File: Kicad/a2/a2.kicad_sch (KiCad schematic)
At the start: 123 parts, among them J1 Conn_02x03_Odd_Even, J2 VGA, J3 AudioJack4, J4 Conn_02x17_Odd_Even, J6 Barrel Jack, J7 DE9_Plug, J8 DE9_Plug, SW1 Q, SW10 P, SW11 A, SW12 S, SW13 D, SW14 F, SW15 G, SW16 H, SW17 J, SW18 K, SW19 L, SW2 W, SW20 ENT, SW21 SHIFT, SW22 Z, SW23 X, SW24 C, SW25 V, SW26 B, SW27 N, SW28 M, SW29 SPACE, SW3 E, SW30 ALT, SW31 SW_Push, SW32 SW_SPDT, SW4 R, SW5 T, SW6 Y, SW7 U, SW8 I, SW9 O, U1 74HC590A, U10 74HC32, U11 74HC174, U12 74HC4520, U2 74HC590A, U3 62256, U4 SST39SF0x0, U5 W65C02SxP, U6 74HCT540, U7 74HC166, U8 74HC14, U9 74HC10, Y1 16Mhz

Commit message: add 2 more m2 screw posts
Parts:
- removed BZ1: Buzzer, Buzzer_Beeper:MagneticBuzzer_Kingstate_KCG0601, symbol Device:Buzzer
- added H5, H6: M2, MountingHole:MountingHole_2.2mm_M2_ISO7380_Pad, symbol Mechanical:MountingHole_Pad
- added LS1: Speaker, Connector_Molex:Molex_PicoBlade_53047-0210_1x02_P1.25mm_Vertical, symbol Device:Speaker
- C16: footprint PCM_Capacitor_THT_AKL:CP_Radial_D5.0mm_P2.00mm -> PCM_Capacitor_THT_AKL:CP_Radial_D4.0mm_P1.50mm
- C17: value 100nF -> 47nF
- H1, H2, H3, H4: value MountingHole_Pad -> M2; now in the parts list
- RN1: value R_Network06 -> 10KΩ
- RN2, RN3: value R_Network04 -> 1KΩ
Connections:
- net DataOut: no longer R6.2
- net GND: now also H5.1, H6.1, LS1.2; no longer C17.2
- net Speaker: now also LS1.1
- net AUDIN renamed DataIn
- new net: C17.2, R6.2
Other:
- moved on the sheet: C13, H1, H2, H3, H4, R6, RN3, SW1, SW10, SW11, SW12, SW13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

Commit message: Big a2 update
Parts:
- removed C14: 100nF, PCM_Capacitor_THT_AKL_Double:C_Disc_D3.0mm_W1.6mm_P2.50mm, symbol Device:C_Small
- removed C3: 4.7µF, PCM_Capacitor_THT_AKL:CP_Radial_D4.0mm_P1.50mm, symbol PCM_Capacitor_AKL:CP_Radial_D5.0mm_P2.00mm
- removed D10, D11, D12, D13, D14, D15, D16, D17, D18, D19, D20, D21, D22, D23, D24, D25, D26, D27, D28, D29, D30, D31, D32, D33, D34, D35, D36, D7, D8, D9: 1N4148, PCM_Diode_THT_AKL_Double:D_DO-35_SOD27_P7.62mm_Horizontal, symbol PCM_Diode_AKL:1N4148
- removed J7, J8: DE9_Plug, Smal:DSUB9-Atari, symbol Connector:DE9_Plug
- removed R3, R4: 27KΩ, PCM_Resistor_THT_AKL_Double:R_Axial_DIN0204_L3.6mm_D1.6mm_P7.62mm_Horizontal, symbol Device:R
- removed R5: 5.6KΩ, PCM_Resistor_THT_AKL_Double:R_Axial_DIN0204_L3.6mm_D1.6mm_P7.62mm_Horizontal, symbol Device:R
- removed RN1: 10KΩ, Resistor_THT:R_Array_SIP7, symbol Device:R_Network06
- removed SW1: Q, MicroMicro:SW_Redragon_MX_LowProfile_PCB_1.00u_Other, symbol Switch:SW_Push_45deg
- removed SW10: P, MicroMicro:SW_Redragon_MX_LowProfile_PCB_1.00u_Other, symbol Switch:SW_Push_45deg
- removed SW11: A, MicroMicro:SW_Redragon_MX_LowProfile_PCB_1.00u_Other, symbol Switch:SW_Push_45deg
- removed SW12: S, MicroMicro:SW_Redragon_MX_LowProfile_PCB_1.00u_Other, symbol Switch:SW_Push_45deg
- removed SW13: D, MicroMicro:SW_Redragon_MX_LowProfile_PCB_1.00u_Other, symbol Switch:SW_Push_45deg
- removed SW14: F, MicroMicro:SW_Redragon_MX_LowProfile_PCB_1.00u_Other, symbol Switch:SW_Push_45deg
- removed SW15: G, MicroMicro:SW_Redragon_MX_LowProfile_PCB_1.00u_Other, symbol Switch:SW_Push_45deg
- removed SW16: H, MicroMicro:SW_Redragon_MX_LowProfile_PCB_1.00u_Other, symbol Switch:SW_Push_45deg
- removed SW17: J, MicroMicro:SW_Redragon_MX_LowProfile_PCB_1.00u_Other, symbol Switch:SW_Push_45deg
- removed SW18: K, MicroMicro:SW_Redragon_MX_LowProfile_PCB_1.00u_Other, symbol Switch:SW_Push_45deg
- removed SW19: L, MicroMicro:SW_Redragon_MX_LowProfile_PCB_1.00u_Other, symbol Switch:SW_Push_45deg
- removed SW2: W, MicroMicro:SW_Redragon_MX_LowProfile_PCB_1.00u_Other, symbol Switch:SW_Push_45deg
- removed SW20: ENT, MicroMicro:SW_Redragon_MX_LowProfile_PCB_1.00u_Other, symbol Switch:SW_Push_45deg
- removed SW21: SHIFT, MicroMicro:SW_Redragon_MX_LowProfile_PCB_1.00u_Other, symbol Switch:SW_Push_45deg
- removed SW22: Z, MicroMicro:SW_Redragon_MX_LowProfile_PCB_1.00u_Other, symbol Switch:SW_Push_45deg
- removed SW23: X, MicroMicro:SW_Redragon_MX_LowProfile_PCB_1.00u_Other, symbol Switch:SW_Push_45deg
- removed SW24: C, MicroMicro:SW_Redragon_MX_LowProfile_PCB_1.00u_Other, symbol Switch:SW_Push_45deg
- removed SW25: V, MicroMicro:SW_Redragon_MX_LowProfile_PCB_1.00u_Other, symbol Switch:SW_Push_45deg
- removed SW26: B, MicroMicro:SW_Redragon_MX_LowProfile_PCB_1.00u_Other, symbol Switch:SW_Push_45deg
- removed SW27: N, MicroMicro:SW_Redragon_MX_LowProfile_PCB_1.00u_Other, symbol Switch:SW_Push_45deg
- removed SW28: M, MicroMicro:SW_Redragon_MX_LowProfile_PCB_1.00u_Other, symbol Switch:SW_Push_45deg
- removed SW29: SPACE, MicroMicro:SW_Redragon_MX_LowProfile_PCB_1.00u_Other, symbol Switch:SW_Push_45deg
- removed SW3: E, MicroMicro:SW_Redragon_MX_LowProfile_PCB_1.00u_Other, symbol Switch:SW_Push_45deg
- removed SW30: ALT, MicroMicro:SW_Redragon_MX_LowProfile_PCB_1.00u_Other, symbol Switch:SW_Push_45deg
- removed SW4: R, MicroMicro:SW_Redragon_MX_LowProfile_PCB_1.00u_Other, symbol Switch:SW_Push_45deg
- removed SW5: T, MicroMicro:SW_Redragon_MX_LowProfile_PCB_1.00u_Other, symbol Switch:SW_Push_45deg
- removed SW6: Y, MicroMicro:SW_Redragon_MX_LowProfile_PCB_1.00u_Other, symbol Switch:SW_Push_45deg
- removed SW7: U, MicroMicro:SW_Redragon_MX_LowProfile_PCB_1.00u_Other, symbol Switch:SW_Push_45deg
- removed SW8: I, MicroMicro:SW_Redragon_MX_LowProfile_PCB_1.00u_Other, symbol Switch:SW_Push_45deg
- removed SW9: O, MicroMicro:SW_Redragon_MX_LowProfile_PCB_1.00u_Other, symbol Switch:SW_Push_45deg
- removed U8: 74HC14, Package_DIP:DIP-14_W7.62mm_LongPads, symbol 74xx:74LS14
- added C17: 100nF, PCM_Capacitor_THT_AKL_Double:C_Disc_D3.0mm_W1.6mm_P2.50mm, symbol Device:C_Small
- added R1: 5.6KΩ, PCM_Resistor_THT_AKL_Double:R_Axial_DIN0204_L3.6mm_D1.6mm_P7.62mm_Horizontal, symbol Device:R
- added U13: MCP100, PCM_Package_TO_SOT_THT_AKL:TO-92, symbol Power_Supervisor:MCP100-475D
- added U8: 74HCT04, Package_DIP:DIP-14_W7.62mm_LongPads, symbol 74xx:74HCT04
- J2: renamed from J4; value Conn_02x17_Odd_Even -> IDC 34
- R3: renamed from R7; footprint PCM_Resistor_THT_AKL_Double:R_Axial_DIN0204_L3.6mm_D1.6mm_P7.62mm_Horizontal -> PCM_Resistor_THT_AKL_Double:R_Axial_DIN0204_L3.6mm_D1.6mm_P5.08mm_Horizontal
- renumbered C11 to C1, C17 to C10, C8 to C11, C10 to C12, C15 to C14, C12 to C15, C13 to C16, C7 to C2, C9 to C3, C6 to C4, C4 to C5, C16 to C6, C1 to C7, C2 to C8, C5 to C9, D41 to D1, D6 to D12, D5 to D13, D1 to D2, D38 to D3, D39 to D4, D40 to D5, D37 to D6, J6 to J1, J1 to J3, J2 to J4, J3 to J5, R1 to R2, R2 to R4, R6 to R5, R8 to R6, RN2 to RN1, RN3 to RN2, SW31 to SW1, SW32 to SW2, U12 to U11, U11 to U12, U4 to U3, U3 to U4
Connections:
- net A0: now also U9.5; no longer U9.11
- net A13: now also U8.13
- net A15: now also U8.11
- net A2: now also U9.4; no longer U9.10
- net A6: now also U8.3
- net GND: now also C4.2, SW1.1, C17.1, U13.3 (VSS), U8.7 (GND); no longer C4.1
- net H32: now also U8.1; no longer U10.1, U12.3 (D0)
- net M16: now also U8.6
- net M2: now also U9.11; no longer U9.5
- net M4: now also U9.10; no longer U9.4
- net M8: now also U9.9; no longer U9.3
- net V512: now also U12.3 (D0), U9.3; no longer U12.11 (D3), U9.9
- net V512*: now also U12.2 (Q0); no longer U12.10 (Q3)
- net VCC: now also C4.1, U7.9 (Clr), C17.2, R1.2, U8.14 (VCC); no longer C4.2, SW1.2
- net ~{A13}: now also U8.12
- net ~{A15}: now also U8.10
- net ~{HSYNC}: now also U12.10 (Q3), U12.13 (D4); no longer U12.12 (Q4), U12.14 (D5)
- net ~{HSYNC}*: now also U12.12 (Q4), U12.14 (D5); no longer J4.13, U12.15 (Q5)
- net ~{RESET}: now also U13.1 (~{RST})
- net ~{sload}: now also U10.3; no longer U1.11 (CPC), U1.13 (CPR), U2.11 (CPC), U2.13 (CPR), U9.6
- net ø1: now also U8.9
- net ø2: now also U8.8
- net Joy 2: now reaches D13.2 (A)
- net ~{HSYNC!}: now reaches U10.11
- net ~{HSYNC!}: now also U12.11 (D3); no longer U12.13 (D4)
- net ~{MRC!}: now reaches U12.4 (D1), U9.12
- net ~{VSYNC!}: now reaches U12.6 (D2)
- net ~{VSYNC!}: now also U9.6; no longer U9.8
- net at C7.1, R4.1, Y1.1: now also U8.5
- net Joy 1: now reaches D12.2 (A)
- net at U10.12: now also U8.4
- net V1: now reaches U2.6 (Q6)
- net COL 0 renamed Col 1
- net COL 1 renamed Col 2
- net COL 2 renamed Col 3
- net COL 3 renamed Col 4
- net COL 4 renamed Col 5
- net H32* renamed ~{load}
- net ~{load}: now also U1.11 (CPC), U1.13 (CPR), U2.11 (CPC), U2.13 (CPR), U9.8; no longer U12.2 (Q0)
- net HROW 0 renamed HRow 1
- net HROW 1 renamed HRow 2
- net HROW 2 renamed HRow 3
- net HROW 3 renamed HRow 4
- net HROW 4 renamed HRow 5
- net HROW 5 renamed HRow 6
- new net: R1.1, SW1.2, U13.2 (VDD)
- new net ~{H32}: U10.1, U8.2
- new net ~{HSYNC}**: J4.13, U12.15 (Q5)
- no-connect marks 16 -> 15
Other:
- added sheet Keyboard and Joysticks (keyboard.kicad_sch)
- note added: "=522, 523"
- note added: "BIOS ROM"
- note added: "INPUT"
- note added: "RAM"
- note added: "VIDEO Hi"
- note added: "VIDEO Lo"
- note added: "VIDEO Out"
- note added: "VIDEO Signal"
- note removed: "32K RAM"
- note removed: "522-523"
- note removed: "8K ROM"
- note removed: "Clock"
- note removed: "Expansion Slot"
- note removed: "H1"
- note removed: "H16"
- note removed: "H2"
- note removed: "H32"
- note removed: "H4"
- note removed: "H8"
- note removed: "Joysticks"
- note removed: "Keyboard"
- note removed: "Pixel Shifter"
- note removed: "Power Input"
- note removed: "Reset"
- note removed: "V1"
- note removed: "V128"
- note removed: "V16"
- note removed: "V2"
- note removed: "V256"
- note removed: "V32"
- note removed: "V4"
- note removed: "V512"
- note removed: "V64"
- note removed: "V8"
- note removed: "Video Counters"
- note removed: "Video Signal Buffer"
- moved on the sheet: C11, C12, C6, C7, C8, D1, H1, H2, H3, H4, H5, H6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

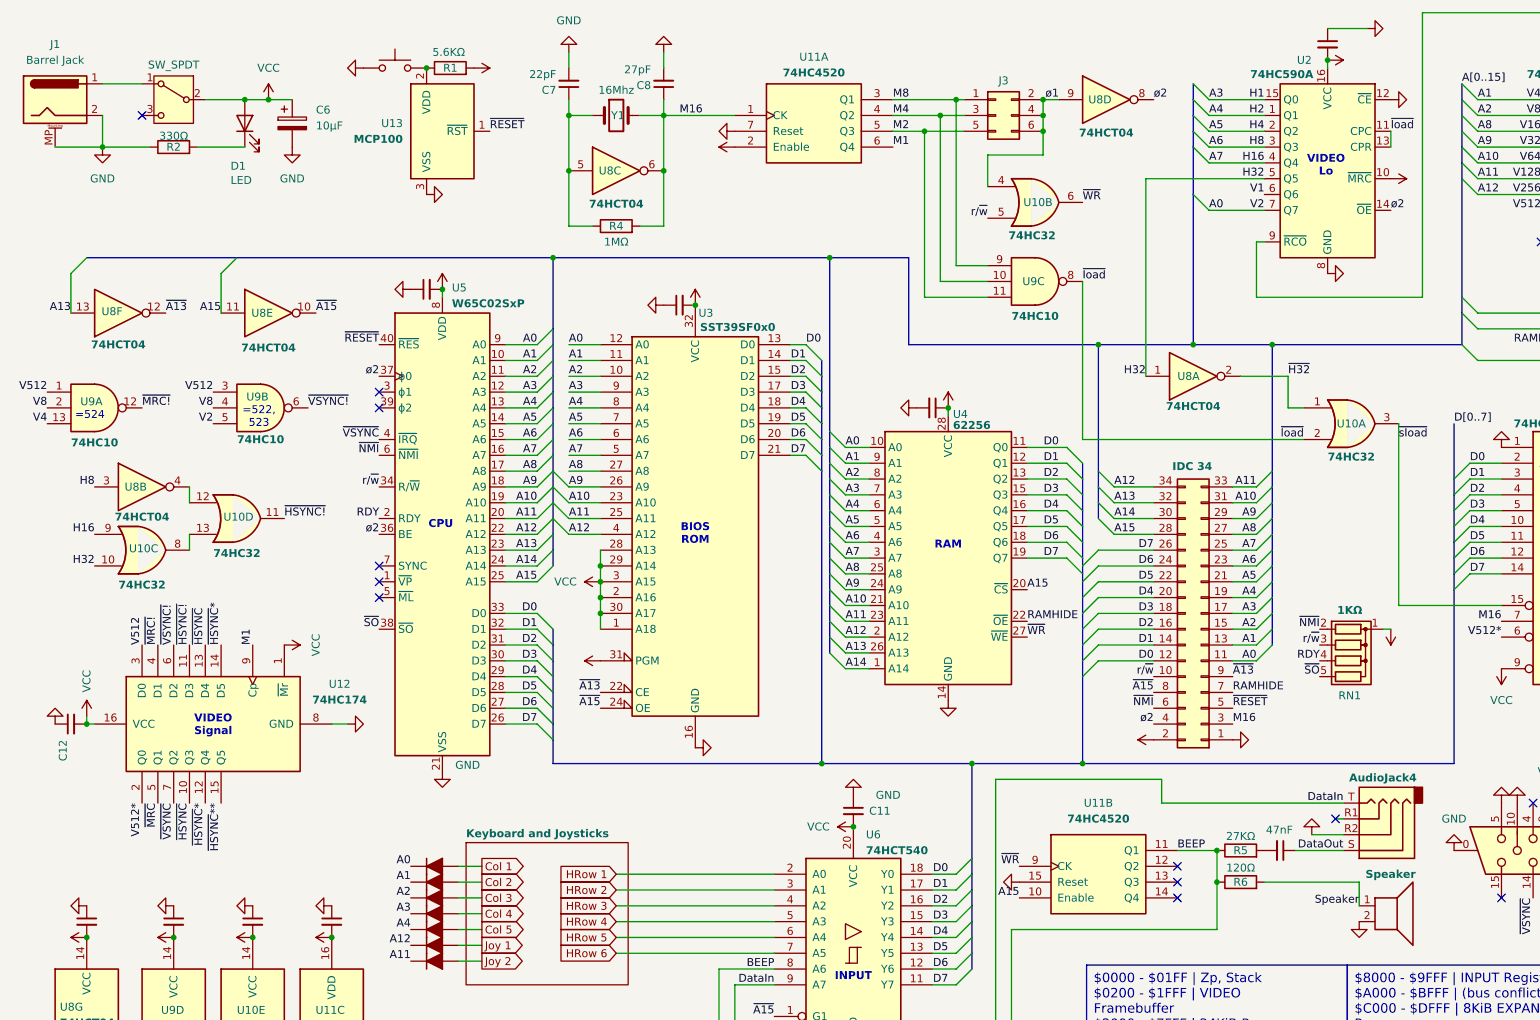
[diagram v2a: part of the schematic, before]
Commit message: Specify MCP100 H boundout version (why are there 2)
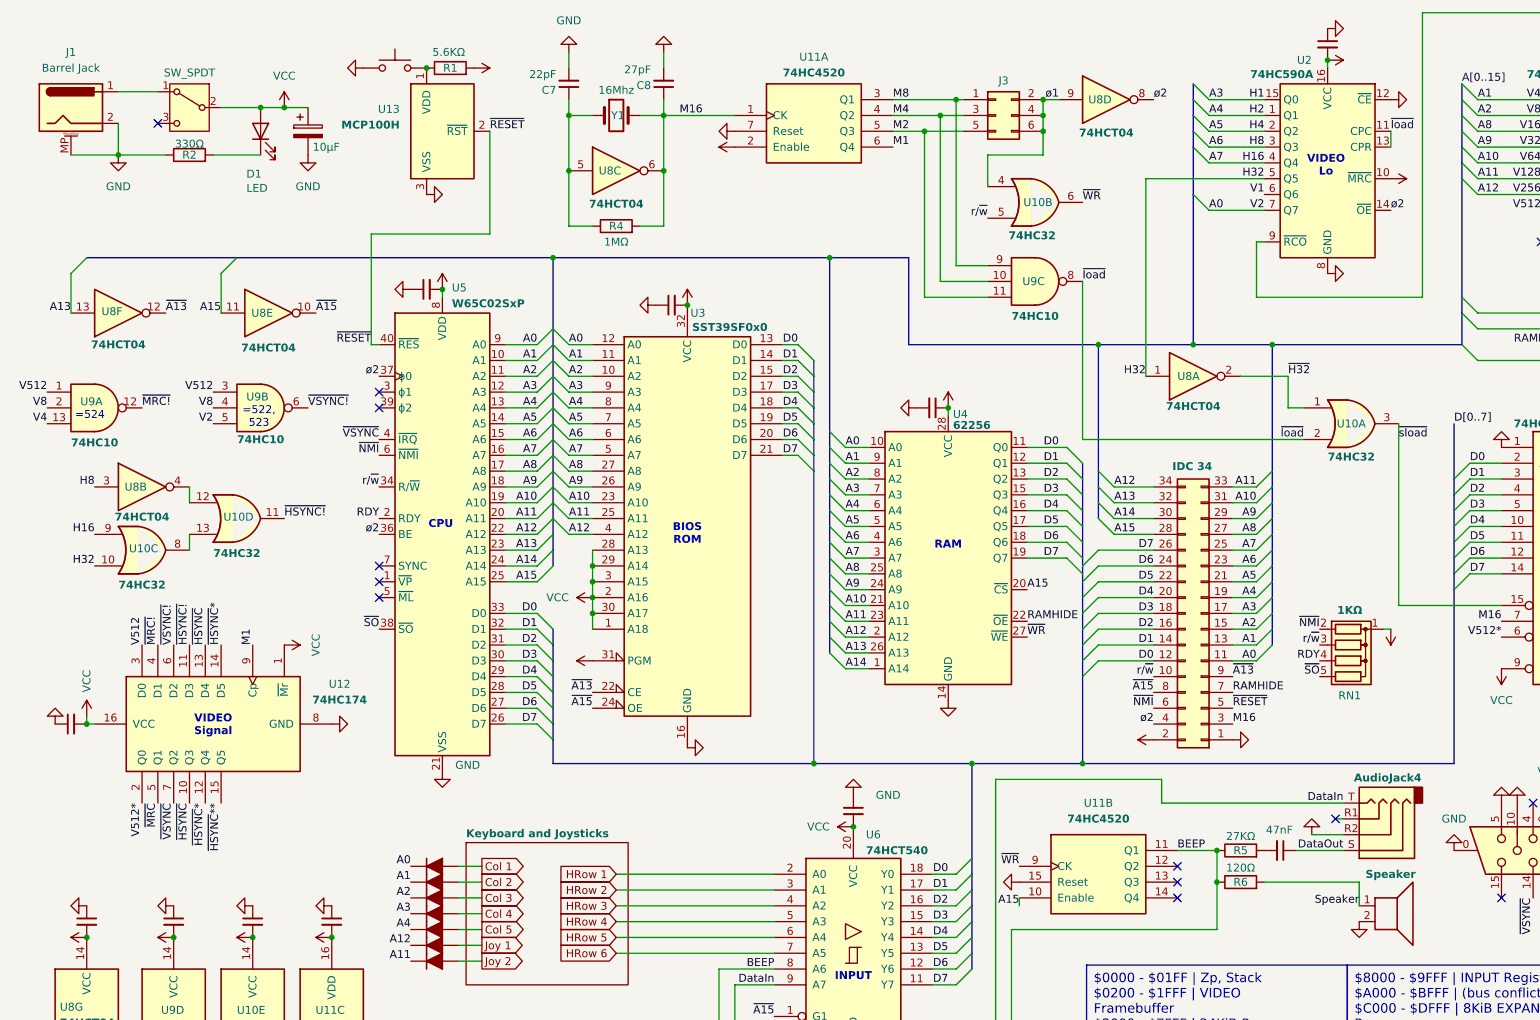
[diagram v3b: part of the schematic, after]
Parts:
- removed U13: MCP100, PCM_Package_TO_SOT_THT_AKL:TO-92, symbol Power_Supervisor:MCP100-475D
- added U13: MCP100H, Package_TO_SOT_THT:TO-92, symbol MM:MCP100H
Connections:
- net GND: now also U13.3 (VSS)
- net ~{RESET}: now also U13.2 (~{RST})
- net at R1.1, SW1.2: now also U13.1 (VDD)
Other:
- moved on the sheet: D1, J1, R2, U3
